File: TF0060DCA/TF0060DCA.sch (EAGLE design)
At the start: 18 parts, among them IC1 LM1972MX_NOPB, IC2 7805T, IC8 LM1117MPX-3.3

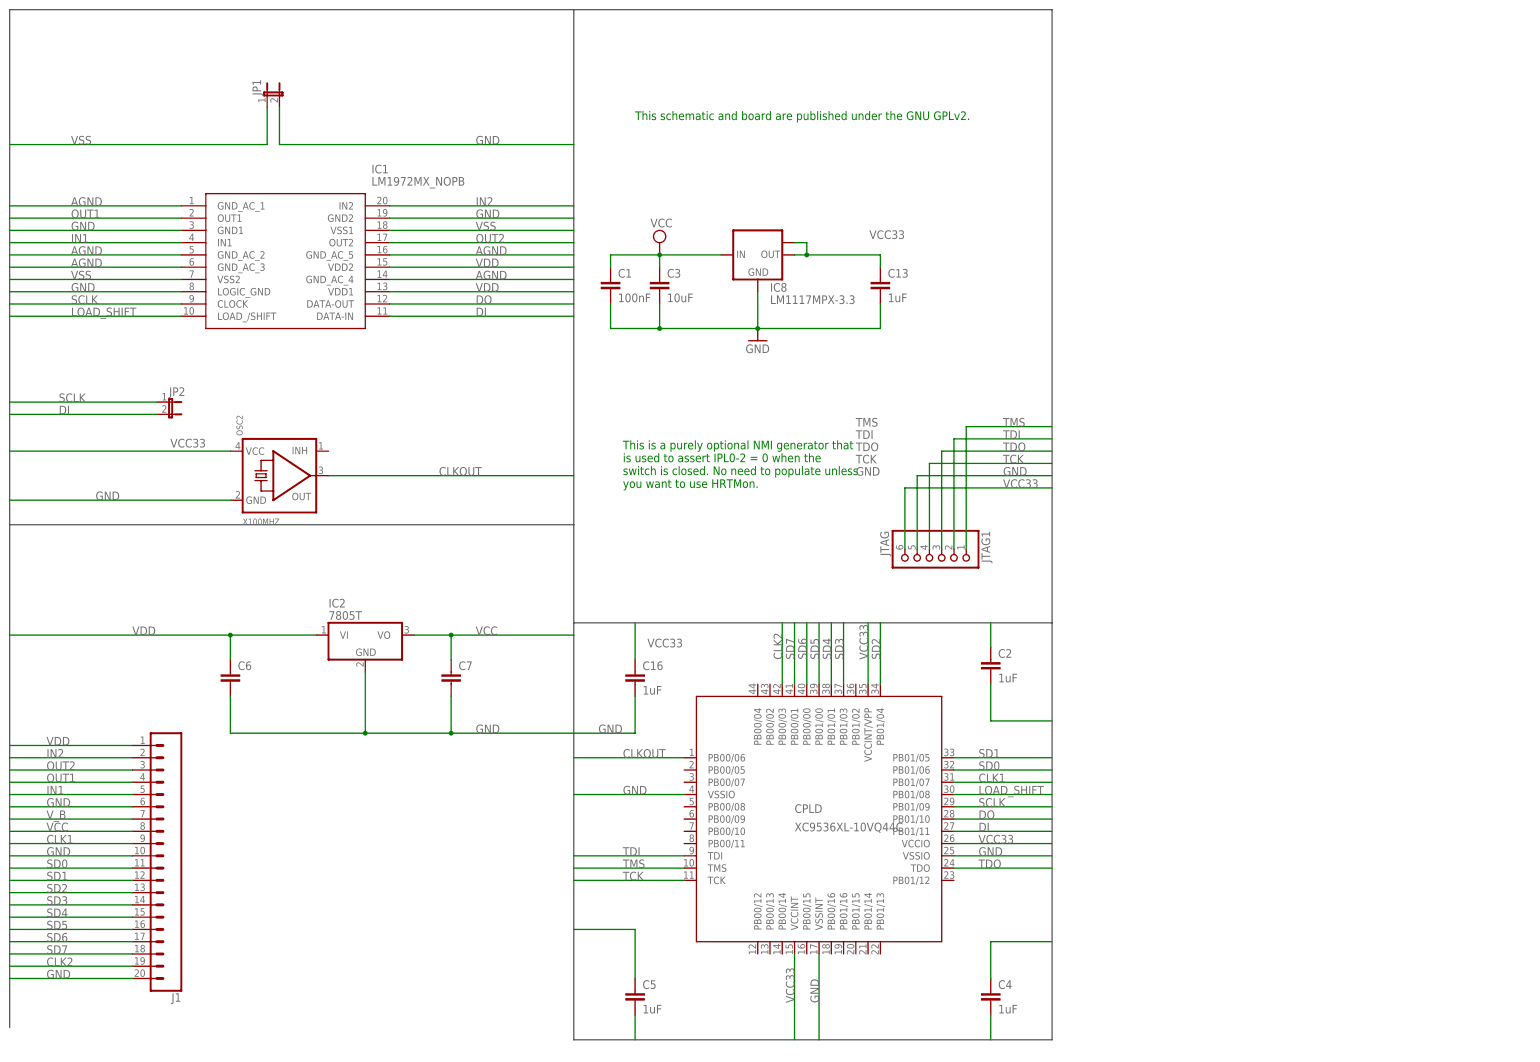
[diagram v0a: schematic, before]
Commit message: upgraded the DC bias
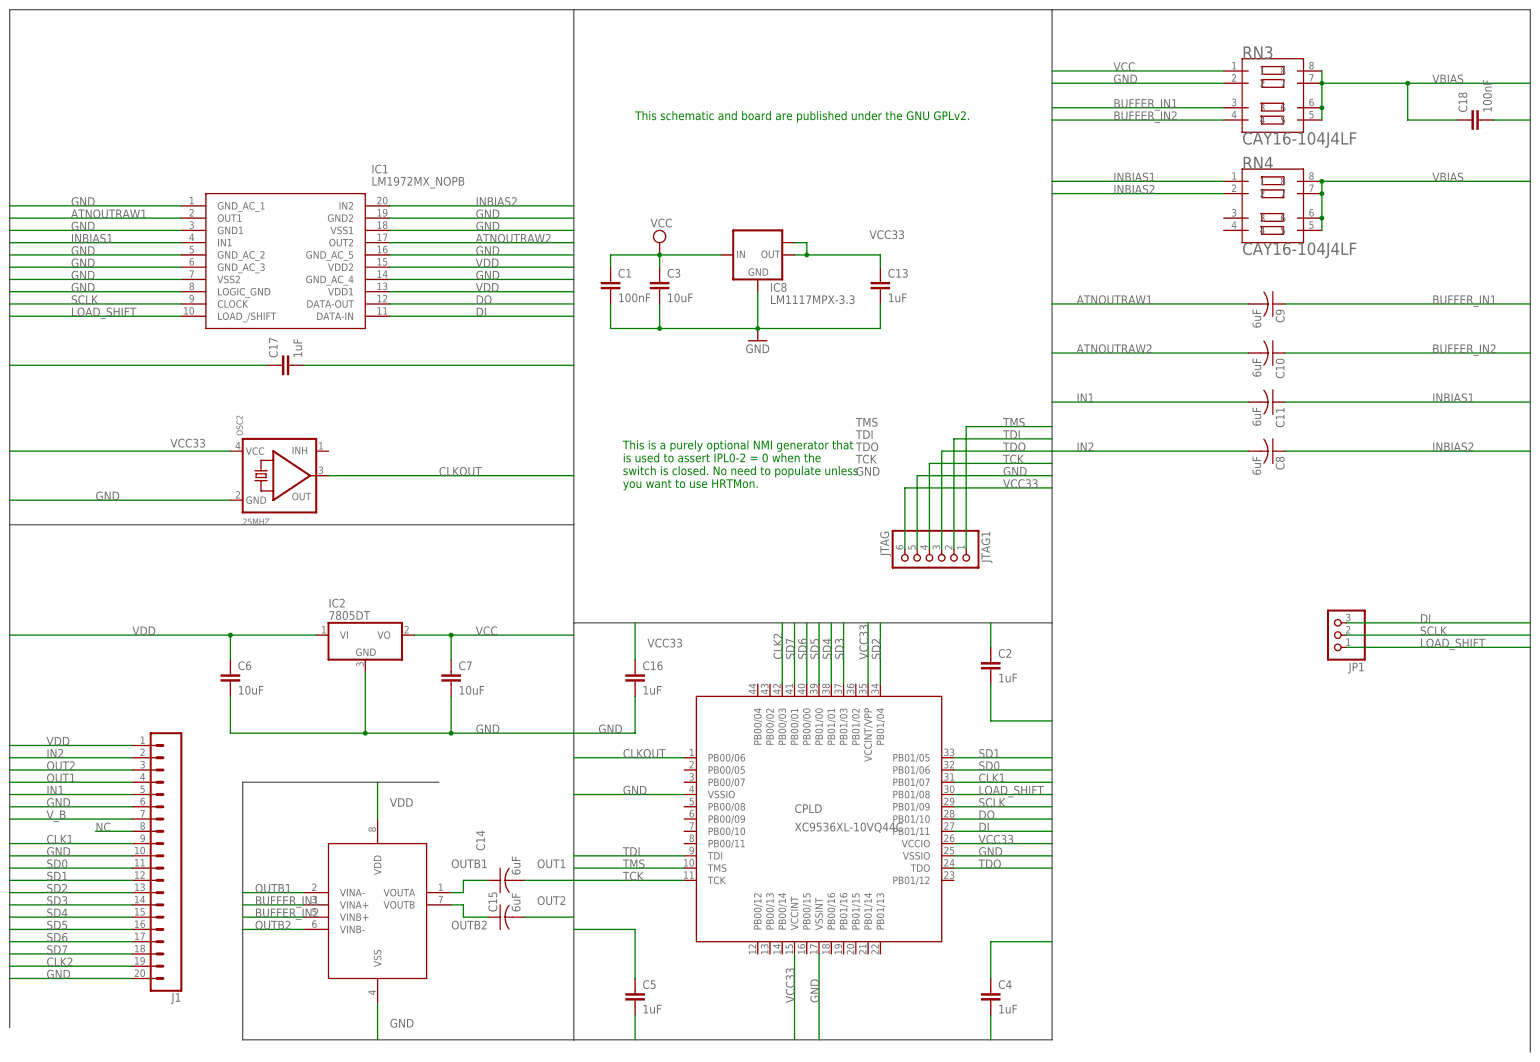
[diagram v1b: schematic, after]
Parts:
- removed JP2: (no value), SparkFun-Retired:JUMPER-2PTH
- added C10, C11, C14, C15, C8, C9: 6uF, rcl:C-USC0805
- added C17: 1uF, eagle-ltspice:CC0603
- added C18: 100nF, eagle-ltspice:CC0603
- added IC12: MCP6002T-I_SN, MCP6002T-I_SN:MCP6002T-I_SN
- added RN3, RN4: CAY16-104J4LF, CAY16-103J4LF:CAY16-103J4LF
- C6, C7: value (none) -> 10uF
- IC2: value 7805T -> 7805DT; device linear:7805T -> linear:7805DT
- JP1: device SparkFun-Retired:JUMPER-2PTH -> adafruit:PINHD-1X3
- OSC2: value X100MHZ -> 25MHZ
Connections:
- removed net AGND: IC1.GND_AC_1, IC1.GND_AC_2, IC1.GND_AC_3, IC1.GND_AC_4, IC1.GND_AC_5
- removed net VSS: IC1.VSS1, IC1.VSS2, JP1.1
- new net ATNOUTRAW1: C9.2, IC1.OUT1
- new net ATNOUTRAW2: C10.2, IC1.OUT2
- new net BUFFER_IN1: C9.1, IC12.VINA+, RN3.3
- new net BUFFER_IN2: C10.1, IC12.VINB+, RN3.4
- new net INBIAS1: C11.1, IC1.IN1, RN4.1
- new net INBIAS2: C8.1, IC1.IN2, RN4.2
- new net NC: J1.8
- new net OUTB1: C14.1, IC12.VINA-, IC12.VOUTA
- new net OUTB2: C15.1, IC12.VINB-, IC12.VOUTB
- new net VBIAS: C18.1, RN3.5, RN3.6, RN3.7, RN3.8, RN4.5, RN4.6, RN4.7, RN4.8
- net DI: now also JP1.3; no longer JP2.2
- net GND: now also C17.2, C18.2, IC1.GND_AC_1, IC1.GND_AC_2, IC1.GND_AC_3, IC1.GND_AC_4, IC1.GND_AC_5, IC1.VSS1, IC1.VSS2, IC12.VSS, RN3.2; no longer JP1.2
- net IN1: now also C11.2; no longer IC1.IN1
- net IN2: now also C8.2; no longer IC1.IN2
- net LOAD_SHIFT: now also JP1.1
- net OUT1: now also C14.2; no longer IC1.OUT1
- net OUT2: now also C15.2; no longer IC1.OUT2
- net SCLK: now also JP1.2; no longer JP2.1
- net VCC: now also C17.1, RN3.1; no longer J1.8
- net VDD: now also IC12.VDD

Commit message: Updated to CH32 control chip
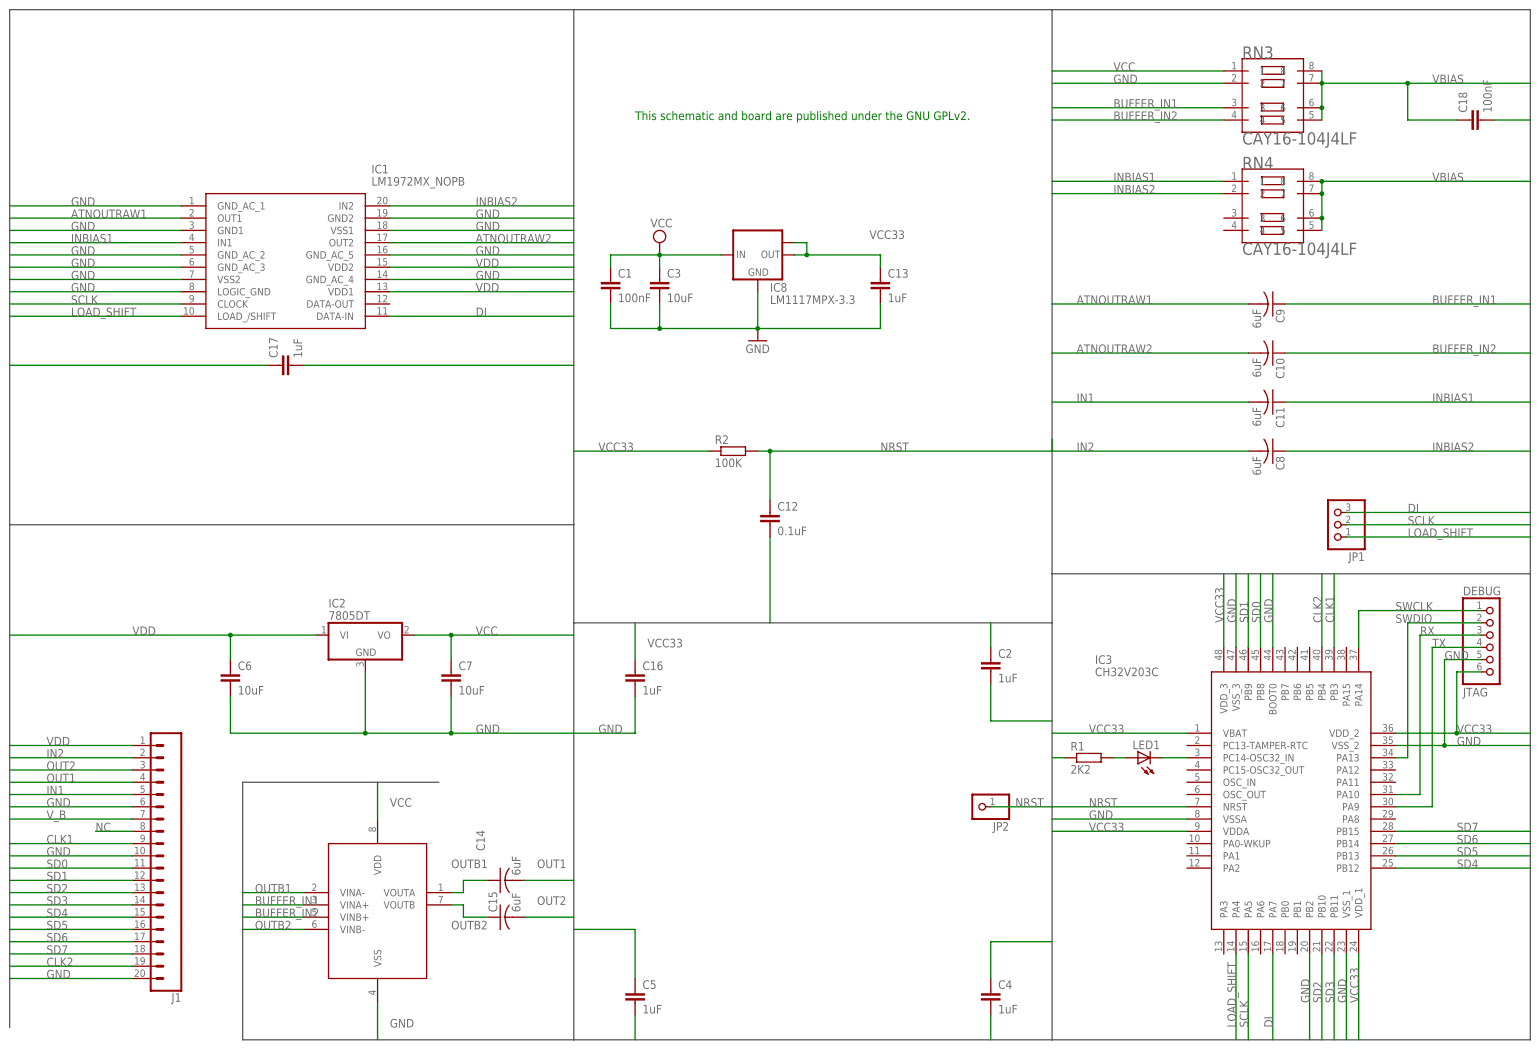
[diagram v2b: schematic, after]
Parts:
- removed CPLD: XC9536XL-10VQ44C, xilinx-xc9:XC9536_44VQ
- removed JTAG1: JTAG, microbuilder:HEADER-1X6ROUND
- removed OSC2: 25MHZ, microbuilder:OSCILLATOR
- added C12: 0.1uF, eagle-ltspice:CC0603
- added DEBUG: JTAG, microbuilder:HEADER-1X6ROUND
- added IC3: CH32V203C, SamacSys_Parts:STM32F103CBT6
- added JP2: (no value), pinhead:PINHD-1X1
- added LED1: (no value), adafruit:LEDCHIPLED_0603
- added R1: 2K2, resistor:R-EU_R0603
- added R2: 100K, resistor:R-EU_R0603
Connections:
- removed net CLKOUT: CPLD.PB00/06, OSC2.OUT
- removed net DO: CPLD.PB01/10, IC1.DATA-OUT
- removed net TCK: CPLD.TCK, JTAG1.4
- removed net TDI: CPLD.TDI, JTAG1.2
- removed net TDO: CPLD.TDO, JTAG1.3
- removed net TMS: CPLD.TMS, JTAG1.1
- new net N$3: IC3.PC14-OSC32_IN, LED1.C
- new net N$4: LED1.A, R1.2
- new net NRST: C12.1, IC3.NRST, JP2.1, R2.2
- new net RX: DEBUG.3, IC3.PA10
- new net SWCLK: DEBUG.1, IC3.PA14
- new net SWDIO: DEBUG.2, IC3.PA13
- new net TX: DEBUG.4, IC3.PA9
- net CLK1: now also IC3.PB3; no longer CPLD.PB01/07
- net CLK2: now also IC3.PB4; no longer CPLD.PB00/03
- net DI: now also IC3.PA7; no longer CPLD.PB01/11
- net GND: now also C12.2, DEBUG.5, IC3.BOOT0, IC3.PB2, IC3.VSSA, IC3.VSS_1, IC3.VSS_2, IC3.VSS_3; no longer CPLD.VSSINT@1, CPLD.VSSIO@1, CPLD.VSSIO@2, JTAG1.5, OSC2.GND
- net LOAD_SHIFT: now also IC3.PA4; no longer CPLD.PB01/08
- net SCLK: now also IC3.PA5; no longer CPLD.PB01/09
- net SD0: now also IC3.PB8; no longer CPLD.PB01/06
- net SD1: now also IC3.PB9; no longer CPLD.PB01/05
- net SD2: now also IC3.PB10; no longer CPLD.PB01/04
- net SD3: now also IC3.PB11; no longer CPLD.PB01/03
- net SD4: now also IC3.PB12; no longer CPLD.PB01/01
- net SD5: now also IC3.PB13; no longer CPLD.PB01/00
- net SD6: now also IC3.PB14; no longer CPLD.PB00/00
- net SD7: now also IC3.PB15; no longer CPLD.PB00/01
- net VCC: now also IC12.VDD
- net VCC33: now also DEBUG.6, IC3.VBAT, IC3.VDDA, IC3.VDD_1, IC3.VDD_2, IC3.VDD_3, R1.1, R2.1; no longer CPLD.VCCINT/VPP, CPLD.VCCINT@1, CPLD.VCCIO@1, JTAG1.6, OSC2.VCC
- net VDD: no longer IC12.VDD
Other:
- note removed: "This is a purely optional NMI generator that is used to assert IPL0-2 = 0 when the switch is closed. No need to populate unless you want to use HRTMon."
- moved on the sheet: JP1
